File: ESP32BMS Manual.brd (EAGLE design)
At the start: 100 x 80 mm, 45 parts, among them J1 RJ11-2L-B, Q1 IRFZ44N, Q2 IRFZ44N, Q3 IRFZ44N, Q4 IRFZ44N, X1 JST-XH-04-PIN-ROUND-PAD

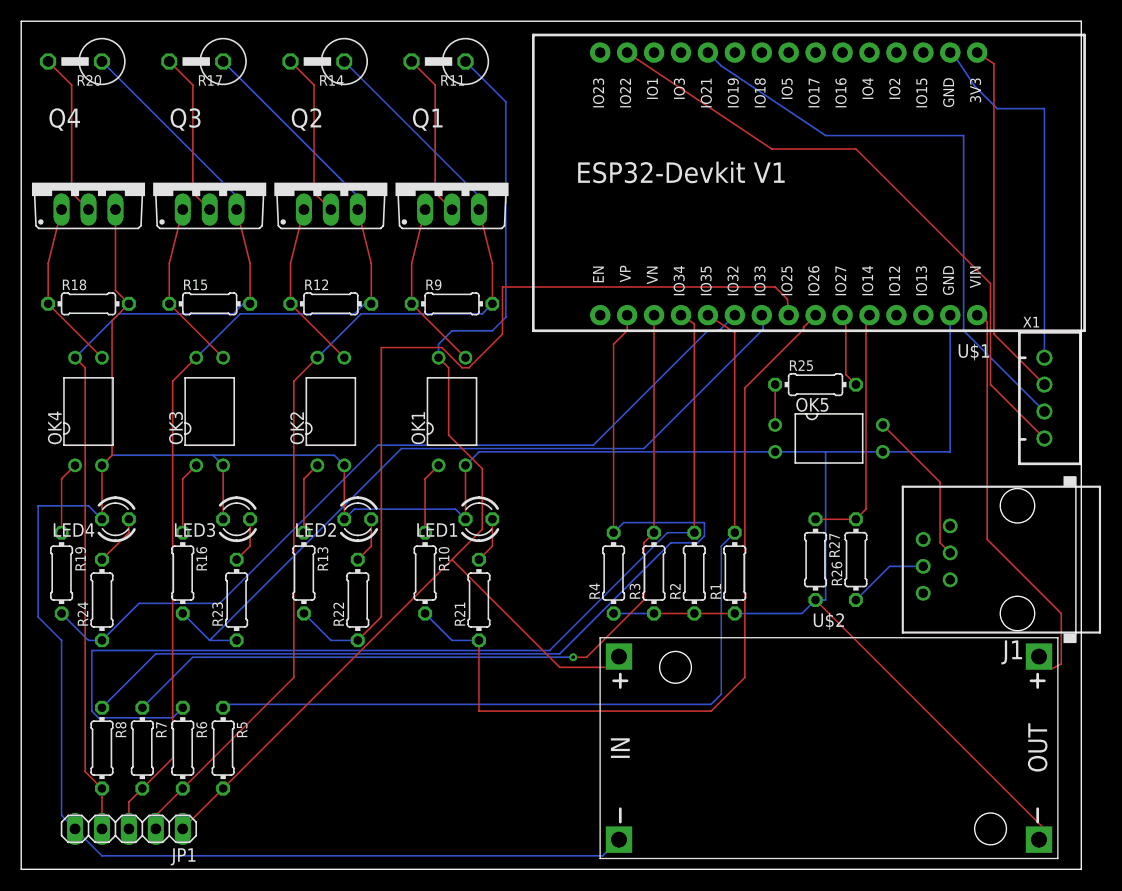
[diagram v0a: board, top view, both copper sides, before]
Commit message: Added mounting holes and widened discharge paths/traces.
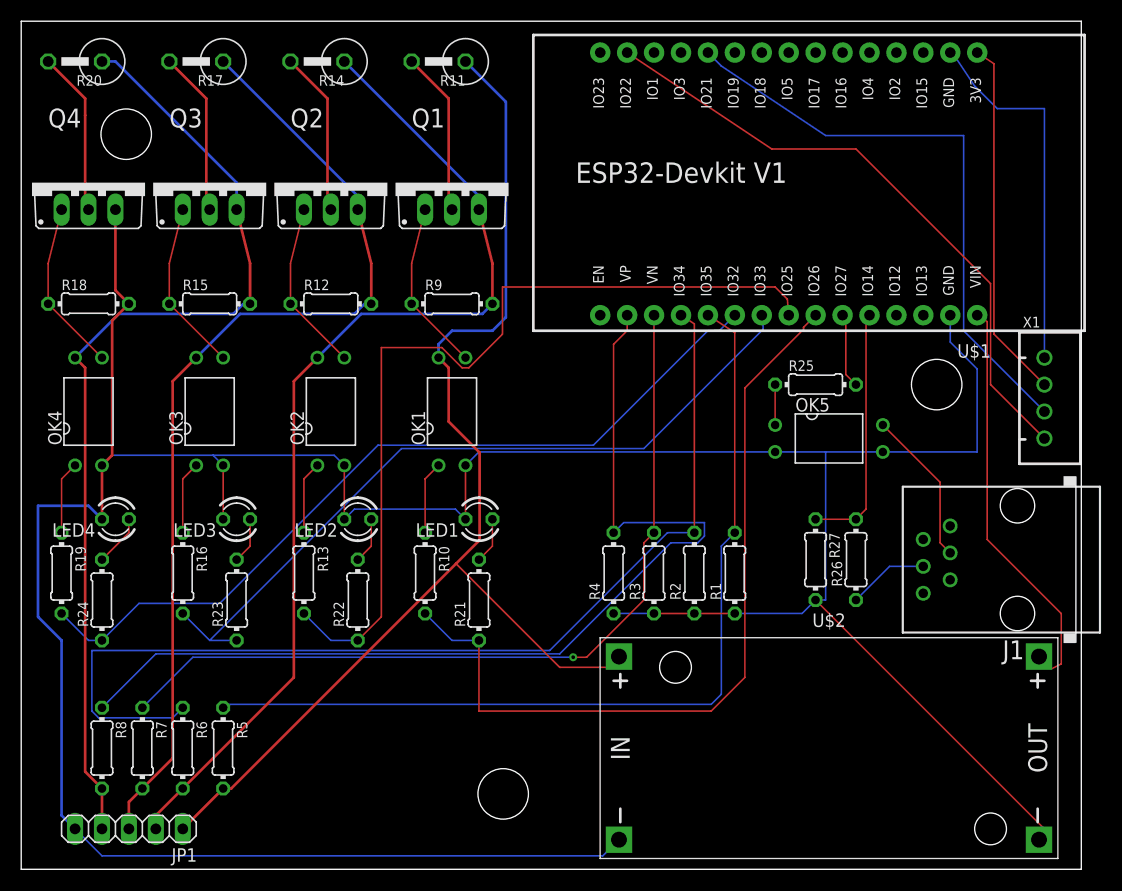
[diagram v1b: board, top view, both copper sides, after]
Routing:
- net GND: track 300.2 -> 303.8 mm
- net N$8: track 92.4 -> 93.1 mm
